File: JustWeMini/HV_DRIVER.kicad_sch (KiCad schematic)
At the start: 12 parts, among them Q2 SSM6L820R, U7 UCC27531DR

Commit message: Feat: minimal changes, added LED, fixed serigraphy
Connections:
- net at U7.6 (VDD): now also C40.2, Q2.3 (D), R26.1

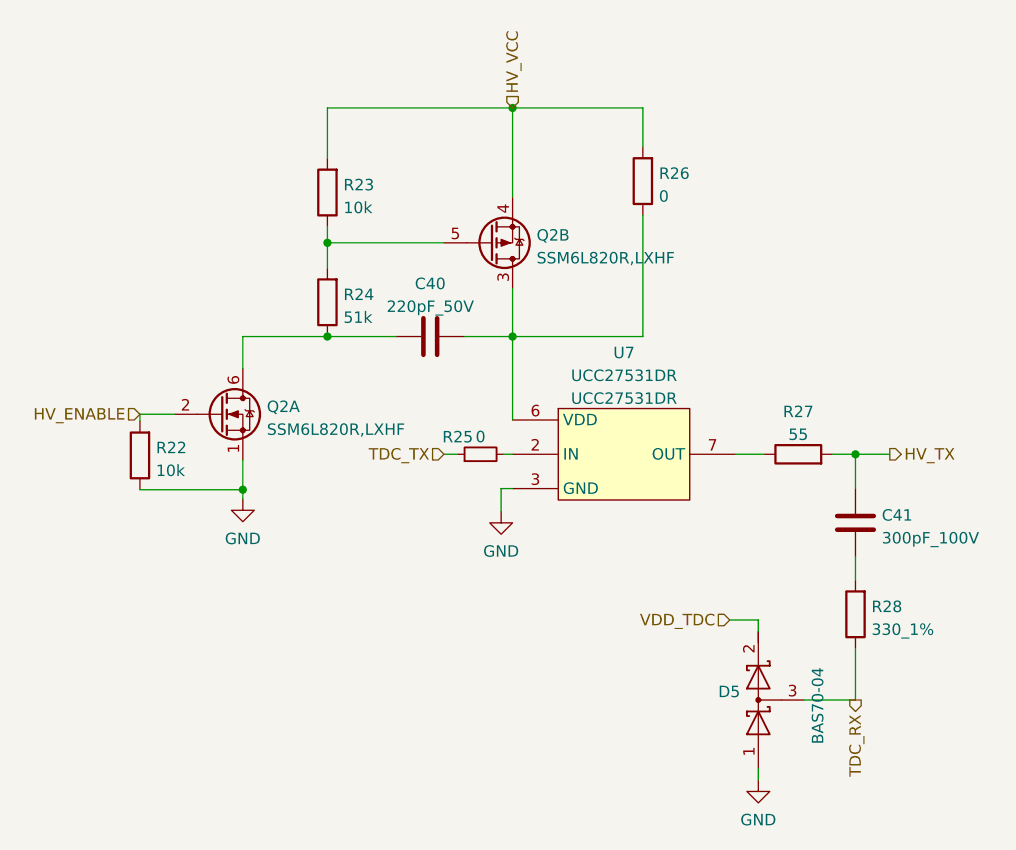
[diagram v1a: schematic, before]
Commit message: Feat: MPN adjusted
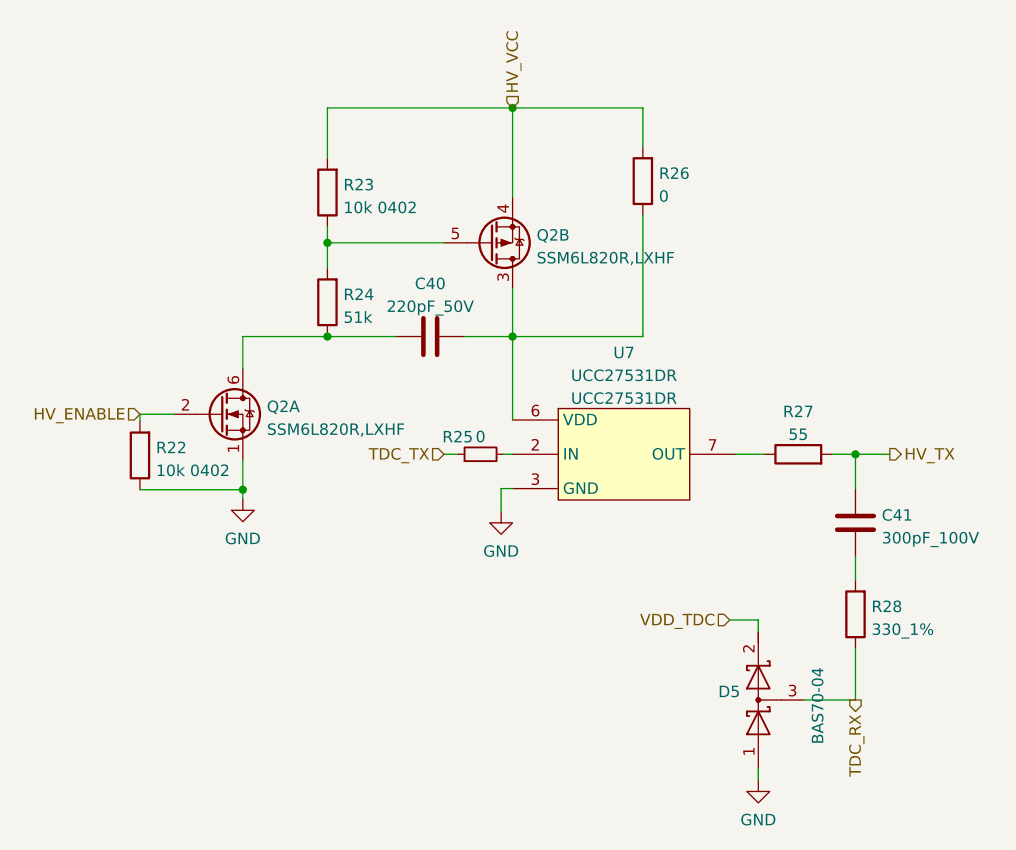
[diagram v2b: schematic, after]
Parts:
- R22, R23: value 10k -> 10k 0402; MPN (none) -> WR04X1002FTL
- R24: MPN (none) -> RC0402JR-0751KL
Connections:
- net at U7.6 (VDD): now also C40.2, Q2.3 (D), R26.1
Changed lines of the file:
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@@
       (effects (font (size 1.27 1.27)) hide)
     )
-    (property "Datasheet" "~" (id 3) (at 194.31 75.565 0)
+    (property "Datasheet" "" (id 3) (at 194.31 75.565 0)
       (effects (font (size 1.27 1.27)) hide)
     )
@@
       (effects (font (size 1.27 1.27)) hide)
     )
-    (property "Datasheet" "~" (id 3) (at 159.004 75.565 0)
+    (property "Datasheet" "" (id 3) (at 159.004 75.565 0)
       (effects (font (size 1.27 1.27)) hide)
     )
@@
       (effects (font (size 1.27 1.27)) hide)
     )
-    (property "Datasheet" "~" (id 3) (at 141.986 58.674 0)
-      (effects (font (size 1.27 1.27)) hide)
-    )
-    (property "MPN" "" (id 4) (at 141.986 58.674 0)
+    (property "Datasheet" "" (id 3) (at 141.986 58.674 0)
+      (effects (font (size 1.27 1.27)) hide)
+    )
+    (property "MPN" "RC0402JR-0751KL" (id 4) (at 141.986 58.674 0)
       (effects (font (size 1.27 1.27)) hide)
     )
@@
       (effects (font (size 1.27 1.27)) hide)
     )
-    (property "Datasheet" "~" (id 3) (at 177.038 45.212 0)
+    (property "Datasheet" "" (id 3) (at 177.038 45.212 0)
       (effects (font (size 1.27 1.27)) hide)
     )
@@
       (effects (font (size 1.27 1.27)) (justify right))
     )
-    (property "Value" "10k" (id 1) (at 143.764 48.1842 0)
+    (property "Value" "10k 0402" (id 1) (at 143.764 48.1842 0)
       (effects (font (size 1.27 1.27)) (justify right))
     )
@@
       (effects (font (size 1.27 1.27)) hide)
     )
-    (property "Datasheet" "~" (id 3) (at 141.986 46.482 0)
-      (effects (font (size 1.27 1.27)) hide)
-    )
-    (property "MPN" "" (id 4) (at 141.986 46.482 0)
+    (property "Datasheet" "" (id 3) (at 141.986 46.482 0)
+      (effects (font (size 1.27 1.27)) hide)
+    )
+    (property "MPN" "WR04X1002FTL" (id 4) (at 141.986 46.482 0)
       (effects (font (size 1.27 1.27)) hide)
     )
@@
       (effects (font (size 1.27 1.27)) (justify right))
     )
-    (property "Value" "10k" (id 1) (at 122.936 77.3942 0)
+    (property "Value" "10k 0402" (id 1) (at 122.936 77.3942 0)
       (effects (font (size 1.27 1.27)) (justify right))
     )
@@
       (effects (font (size 1.27 1.27)) hide)
     )
-    (property "Datasheet" "~" (id 3) (at 121.158 75.692 0)
-      (effects (font (size 1.27 1.27)) hide)
-    )
-    (property "MPN" "" (id 4) (at 121.158 75.692 0)
-      (effects (font (size 1.27 1.27)) hide)
-    )
+    (property "Datasheet" "" (id 3) (at 121.158 75.692 0)
+      (effects (font (size 1.27 1.27)) hide)
+    )
+    (property "MPN" "WR04X1002FTL" (id 4) (at 121.158 75.692 0)
+      (effects (font (size 1.27 1.27)) hide)
+    )
